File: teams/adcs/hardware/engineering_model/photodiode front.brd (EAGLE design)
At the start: 27.3 x 50.2 mm, 15 parts, among them U1 LTC2483IDD

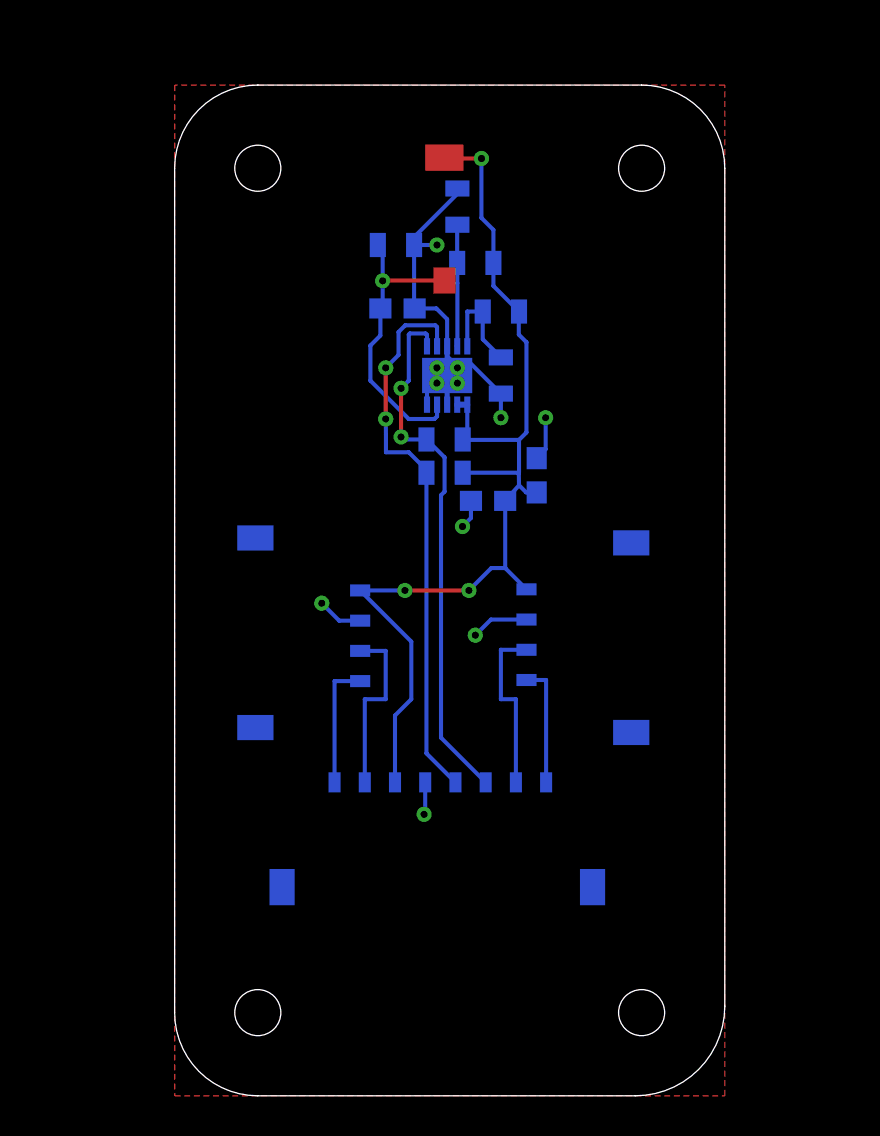
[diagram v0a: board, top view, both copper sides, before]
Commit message: Fixed front photodiode board
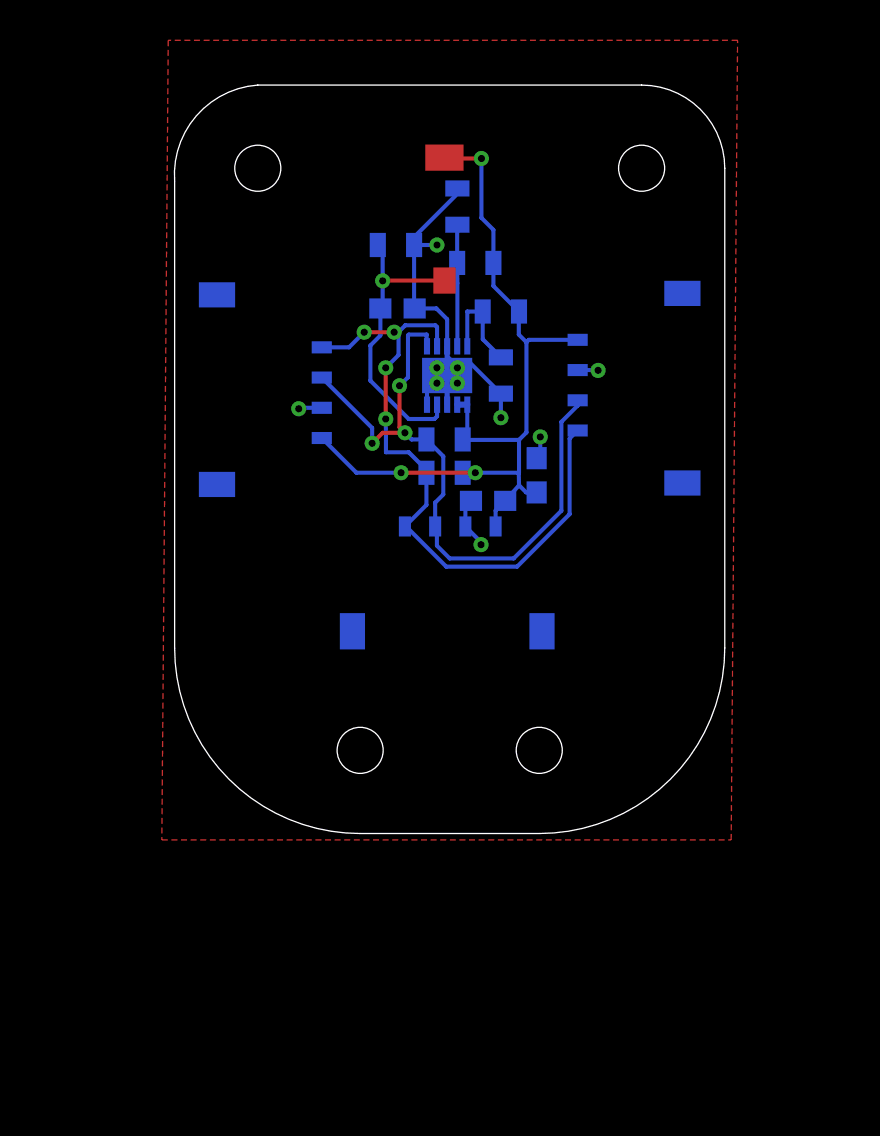
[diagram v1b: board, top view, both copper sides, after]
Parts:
- U$3: value PICOLOCK_8 -> PICOLOCK_4PICOLOCK_4; device DubSat1 Components:PICOLOCK_8 -> DubSat1 Components:PICOLOCK_4
- moved U$3 13.2 mm to (5.40, 13.3)
- moved U$2 12.6 mm to (14.0, 18.1)
- moved U$4 12.2 mm to (1.27, 22.2)
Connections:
- removed net N$1: U$3.P$2, U$4.P$3
- removed net N$2: U$3.P$1, U$4.P$4
- removed net N$3: U$2.P$1, U$3.P$8
- removed net N$4: U$2.P$2, U$3.P$7
- net GND: now also U$3.P$3, U$4.P$3; no longer U$3.P$4, U$4.P$2
- net SCL: now also U$2.P$2, U$3.P$2, U$4.P$2; no longer U$3.P$6
- net SDA: now also U$2.P$1, U$3.P$1, U$4.P$1; no longer U$3.P$5
- net VCC: now also U$3.P$4, U$4.P$4; no longer U$3.P$3, U$4.P$1
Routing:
- net VCC: track 53.7 -> 42.7 mm
- net N$1: track 8.84 -> 0.00 mm
- net N$4: track 8.59 -> 0.00 mm
- net SCL: track 26.5 -> 33.1 mm, vias 2 -> 3
- net N$2: track 6.29 -> 0.00 mm
- net N$3: track 6.05 -> 0.00 mm
- net SDA: track 27.8 -> 33.7 mm, vias 2 -> 4
- net GND: track 31.5 -> 27.2 mm, vias 11 -> 10
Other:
- board size 27.3 x 50.2 mm -> 27.3 x 37.1 mm

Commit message: Photodiode front board changes: same hole locations as before, 2x extra picolock connectors to go to side boards, capacitors changed from 0603 to 0805, smoothing capacitors moved next to power input of ADC, and i2c pullups moved onto the top of the board to be easily removed
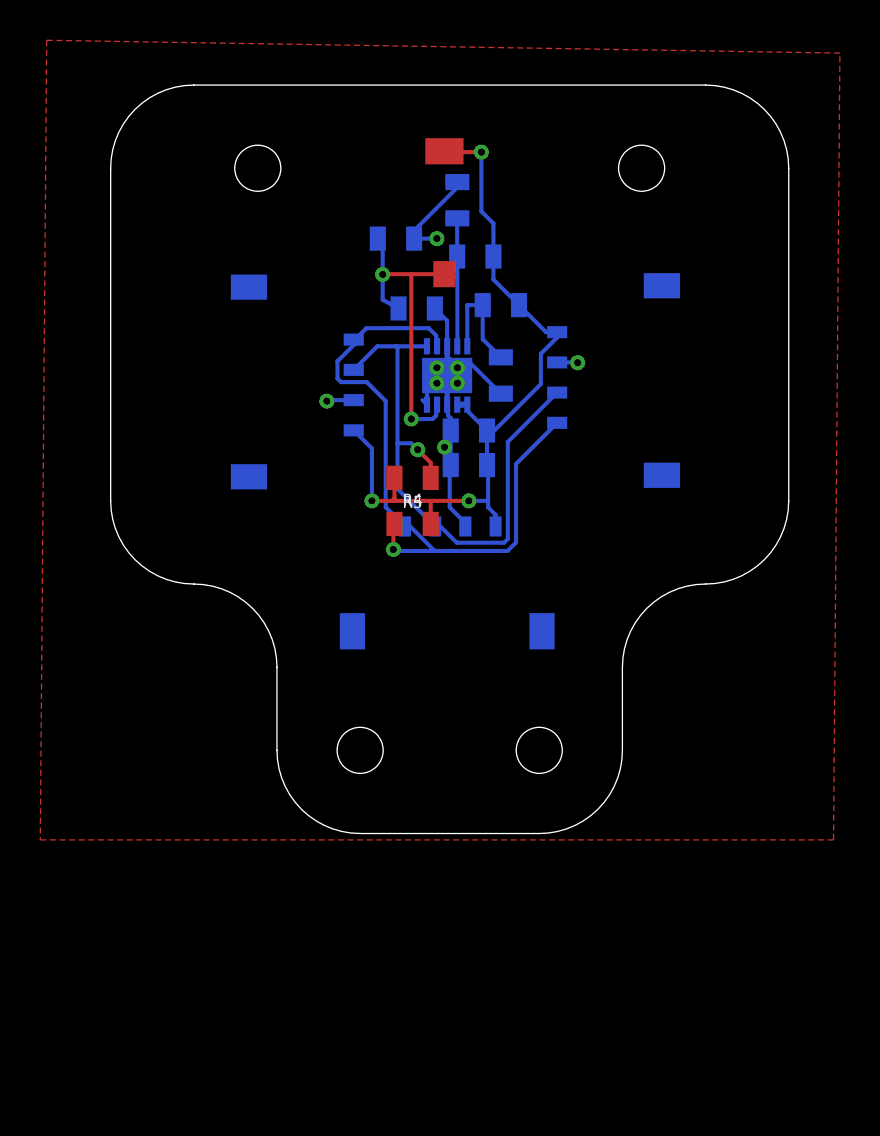
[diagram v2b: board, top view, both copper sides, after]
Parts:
- C1, C6: device SparkFun-Capacitors:0603 -> SparkFun-Capacitors:0805
- C2: value 1uF -> 1.0uF; device SparkFun-Capacitors:0603 -> SparkFun-Capacitors:0805
- moved C1 3.62 mm to (8.57, 18.1)
- moved C2 3.40 mm to (8.57, 16.4), turned to 0 degrees
- moved R4 3.00 mm to (5.78, 13.5), flipped to the top, turned to 0 degrees
- moved R5 2.48 mm to (5.78, 15.7), flipped to the top
- moved U$4 1.63 mm to (2.86, 22.6)
- moved U$2 1.09 mm to (13.0, 18.5)
- moved C6 0.95 mm to (5.98, 24.2)
- moved U$1 0.32 mm to (7.30, 26.0)
- moved R1 0.32 mm to (8.00, 29.5)
- moved R2 0.32 mm to (8.89, 26.7)
- moved R3 0.32 mm to (4.95, 27.6)
- moved R6 0.32 mm to (10.2, 24.3)
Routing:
- net SCL: track 33.1 -> 29.0 mm, vias 3 -> 1
- net VCC: track 42.7 -> 39.6 mm
- net GND: track 27.2 -> 24.9 mm, vias 10 -> 8
- net OUTPUT: track 14.9 -> 16.2 mm, vias 1 -> 2
- net CA0: track 5.14 -> 5.78 mm
- net SDA: track 33.7 -> 33.1 mm, vias 4 -> 1
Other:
- board size 27.3 x 37.1 mm -> 33.7 x 37.1 mm
